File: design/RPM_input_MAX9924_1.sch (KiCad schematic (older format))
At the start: 7 parts, among them U30 MAX9924

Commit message: Footprints added to components fields
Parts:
- R215, R216: footprint SM0805 -> SM1210
- R261: footprint (none) -> SM0805
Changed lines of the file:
@@
-EESchema Schematic File Version 2  date Thu 17 Mar 2011 02:57:02 AM ART
+EESchema Schematic File Version 2  date Thu 17 Mar 2011 12:20:05 PM ART
 LIBS:power
 LIBS:freeEMS_lib
@@
 F 0 "R261" V 6980 3350 50  0000 C CNN
 F 1 "1.6k" V 6900 3350 50  0000 C CNN
+F 2 "SM0805" H 6900 3350 60  0001 C CNN
 	1    6900 3350
 	0    1    1    0
@@
 F 0 "R212" V 3380 2800 50  0000 C CNN
 F 1 "10k 1/2W" V 3300 2800 50  0000 C CNN
-F 2 "SM0805" V 1130 2600 60  0001 C CNN
+F 2 "SM1210" V 1130 2600 60  0001 C CNN
 F 4 "Stackpole" V 1130 2600 60  0001 C CNN "mfg"
 F 5 "RMCF0805JT10K0CT" V 1130 2600 60  0001 C CNN "mfg#"
@@
 F 0 "R213" V 3380 3200 50  0000 C CNN
 F 1 "10k 1/2W" V 3300 3200 50  0000 C CNN
-F 2 "SM0805" V 1130 2600 60  0001 C CNN
+F 2 "SM1210" V 1130 2600 60  0001 C CNN
 F 4 "Stackpole" V 1130 2600 60  0001 C CNN "mfg"
 F 5 "RMCF0805JT10K0CT" V 1130 2600 60  0001 C CNN "mfg#"

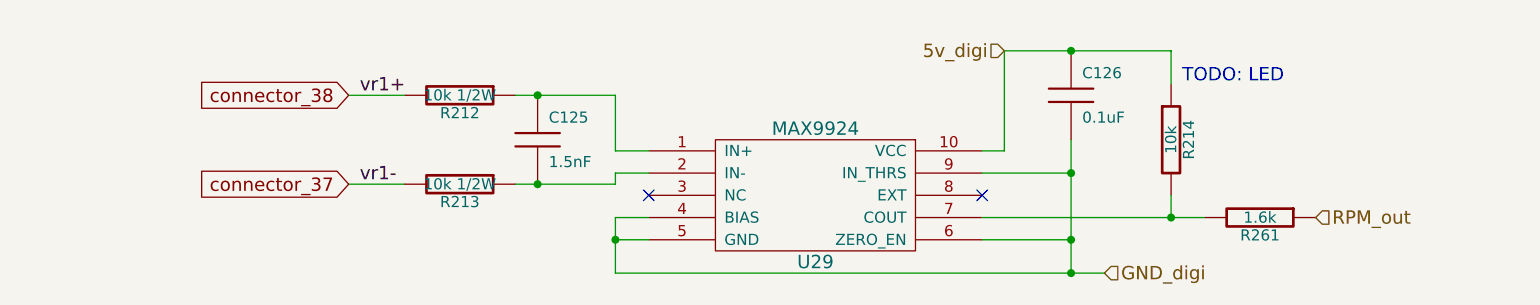
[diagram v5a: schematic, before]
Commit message: Added leds to RPM inputs
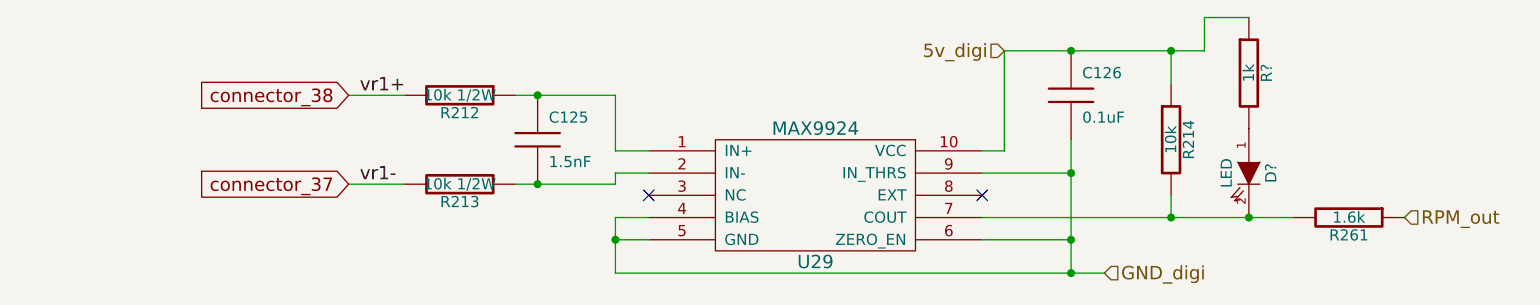
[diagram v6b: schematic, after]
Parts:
- added D?: LED, symbol LED
- added R?: 1k, symbol R
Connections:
- net 5v_digi: now also R?.1
- net at R217.2, R261.2, U30.7 (COUT): now also D?.2 (K)
- new net: D?.1 (A), R?.2
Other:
- note removed: "TODO: LED"
- moved on the sheet: R261
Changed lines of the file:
@@
-EESchema Schematic File Version 2  date Sat 19 Mar 2011 03:00:13 PM ART
+EESchema Schematic File Version 2  date Mon 21 Mar 2011 04:08:08 AM ART
 LIBS:power
 LIBS:freeEMS_lib
@@
 EELAYER END
 $Descr A4 11700 8267
-Sheet 18 55
+Sheet 19 55
 Title "Puma board"
-Date "19 mar 2011"
+Date "21 mar 2011"
 Rev "v0.02"
 Comp "diyefi.org"
@@
 Comment4 ""
 $EndDescr
-Text Notes 6550 2750 0    60   ~ 0
-TODO: LED
+Connection ~ 6850 3350
+Wire Wire Line
+	7050 3350 5650 3350
+Connection ~ 6500 2600
+Wire Wire Line
+	6650 2600 5750 2600
+Wire Wire Line
+	6650 2600 6650 2450
+Wire Wire Line
+	6650 2450 6850 2450
+Wire Wire Line
+	6050 3600 6050 3000
+Wire Wire Line
+	4000 3350 4000 3600
+Wire Wire Line
+	2800 3200 3050 3200
+Wire Wire Line
+	4000 3050 4000 2800
+Wire Wire Line
+	4000 3050 4150 3050
+Wire Wire Line
+	4000 3150 4000 3200
+Wire Wire Line
+	4000 3150 4150 3150
+Connection ~ 6500 3350
+Wire Wire Line
+	6500 3250 6500 3350
+Connection ~ 6050 3450
+Wire Wire Line
+	6050 3150 5650 3150
+Wire Wire Line
+	4000 3450 4150 3450
+Wire Wire Line
+	5650 3050 5750 3050
+Wire Wire Line
+	5750 3050 5750 2600
+Wire Wire Line
+	4000 3350 4150 3350
+Connection ~ 4000 3450
+Wire Wire Line
+	6050 3450 5650 3450
+Connection ~ 6050 3150
+Wire Wire Line
+	6500 2600 6500 2750
+Connection ~ 6050 2600
+Wire Wire Line
+	4000 3200 3550 3200
+Connection ~ 3650 3200
+Wire Wire Line
+	4000 2800 3550 2800
+Connection ~ 3650 2800
+Wire Wire Line
+	3050 2800 2800 2800
+Wire Wire Line
+	4000 3600 6200 3600
+Connection ~ 6050 3600
+$Comp
+L LED D?
+U 1 1 4D86F760
+P 6850 3150
+F 0 "D?" H 6850 3250 50  0000 C CNN
+F 1 "LED" H 6850 3050 50  0000 C CNN
+	1    6850 3150
+	0    1    1    0
+$EndComp
+$Comp
+L R R?
+U 1 1 4D86F74F
+P 6850 2700
+F 0 "R?" V 6930 2700 50  0000 C CNN
+F 1 "1k" V 6850 2700 50  0000 C CNN
+	1    6850 2700
+	1    0    0    -1
+$EndComp
 $Comp
 L R R261
 U 1 1 4D6402A4
-P 6900 3350
-F 0 "R261" V 6980 3350 50  0000 C CNN
-F 1 "1.6k" V 6900 3350 50  0000 C CNN
-F 2 "SM0805" H 6900 3350 60  0001 C CNN
-	1    6900 3350
+P 7300 3350
+F 0 "R261" V 7380 3350 50  0000 C CNN
+F 1 "1.6k" V 7300 3350 50  0000 C CNN
+F 2 "SM0805" H 7300 3350 60  0001 C CNN
+	1    7300 3350
 	0    1    1    0
 $EndComp
@@
 Text HLabel 6200 3600 2    60   Input ~ 0
 GND_digi
-Connection ~ 6050 3600
-Wire Wire Line
-	6200 3600 4000 3600
-Wire Wire Line
-	3050 2800 2800 2800
-Connection ~ 3650 2800
-Wire Wire Line
-	3550 2800 4000 2800
-Connection ~ 3650 3200
-Wire Wire Line
-	3550 3200 4000 3200
-Connection ~ 6050 2600
-Wire Wire Line
-	6500 2750 6500 2600
-Wire Wire Line
-	6500 2600 5750 2600
-Wire Wire Line
-	5650 3350 6650 3350
-Connection ~ 6050 3150
-Wire Wire Line
-	6050 3450 5650 3450
-Connection ~ 4000 3450
-Wire Wire Line
-	4150 3350 4000 3350
-Wire Wire Line
-	5750 2600 5750 3050
-Wire Wire Line
-	5750 3050 5650 3050
-Wire Wire Line
-	4000 3450 4150 3450
-Wire Wire Line
-	6050 3150 5650 3150
-Connection ~ 6050 3450
-Wire Wire Line
-	6500 3250 6500 3350
-Connection ~ 6500 3350
-Wire Wire Line
-	4150 3150 4000 3150
-Wire Wire Line
-	4000 3150 4000 3200
-Wire Wire Line
-	4150 3050 4000 3050
-Wire Wire Line
-	4000 3050 4000 2800
-Wire Wire Line
-	2800 3200 3050 3200
-Wire Wire Line
-	4000 3350 4000 3600
-Wire Wire Line
-	6050 3600 6050 3000
-Text HLabel 7150 3350 2    60   Input ~ 0
+Text HLabel 7550 3350 2    60   Input ~ 0
 RPM_out
 Text HLabel 5750 2600 0    60   Input ~ 0

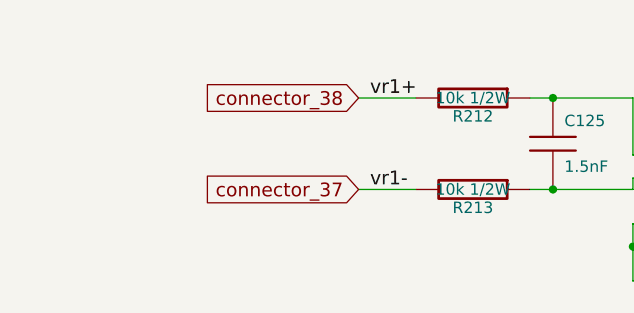
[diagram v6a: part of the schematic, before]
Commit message: Added front-side capacitors on RPM circuits
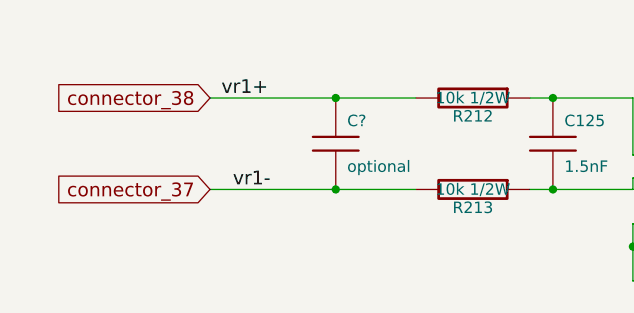
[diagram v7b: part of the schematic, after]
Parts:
- added C?: optional, symbol C
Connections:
- net connector_37: now also C?.2
- net connector_38: now also C?.1
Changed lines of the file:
@@
-EESchema Schematic File Version 2  date Mon 21 Mar 2011 04:08:08 AM ART
+EESchema Schematic File Version 2  date Tue 22 Mar 2011 12:18:09 AM ART
 LIBS:power
 LIBS:freeEMS_lib
@@
 Sheet 19 55
 Title "Puma board"
-Date "21 mar 2011"
+Date "22 mar 2011"
 Rev "v0.02"
 Comp "diyefi.org"
@@
 Comment4 ""
 $EndDescr
+Connection ~ 2700 3200
+Wire Wire Line
+	2150 2800 3050 2800
 Connection ~ 6850 3350
 Wire Wire Line
@@
 Wire Wire Line
 	4000 3350 4000 3600
-Wire Wire Line
-	2800 3200 3050 3200
 Wire Wire Line
 	4000 3050 4000 2800
@@
 Connection ~ 3650 2800
 Wire Wire Line
-	3050 2800 2800 2800
-Wire Wire Line
 	4000 3600 6200 3600
 Connection ~ 6050 3600
+Wire Wire Line
+	2150 3200 3050 3200
+Connection ~ 2700 2800
+$Comp
+L C C?
+U 1 1 4D881199
+P 2700 3000
+F 0 "C?" H 2750 3100 50  0000 L CNN
+F 1 "optional" H 2750 2900 50  0000 L CNN
+	1    2700 3000
+	1    0    0    -1
+$EndComp
 $Comp
 L LED D?
@@
 	0    1    1    0
 $EndComp
-Text Label 2850 3200 0    60   ~ 0
+Text Label 2250 3200 0    60   ~ 0
 vr1-
-Text Label 2850 2800 0    60   ~ 0
+Text Label 2200 2800 0    60   ~ 0
 vr1+
-Text GLabel 2800 2800 0    60   Input ~ 0
+Text GLabel 2150 2800 0    60   Input ~ 0
 connector_38
-Text GLabel 2800 3200 0    60   Input ~ 0
+Text GLabel 2150 3200 0    60   Input ~ 0
 connector_37
 Text HLabel 6200 3600 2    60   Input ~ 0

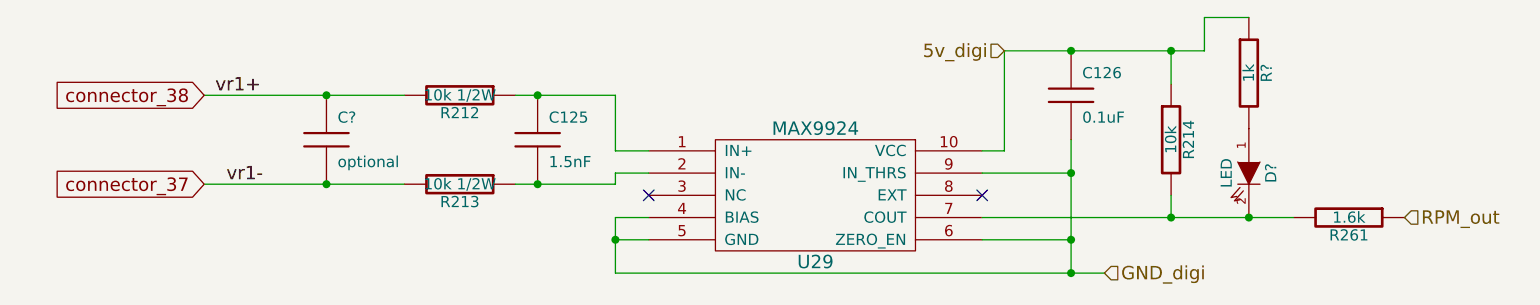
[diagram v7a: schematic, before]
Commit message: Replaced 1/2W resistors by a couple of 1/4W (RPM circuitry)
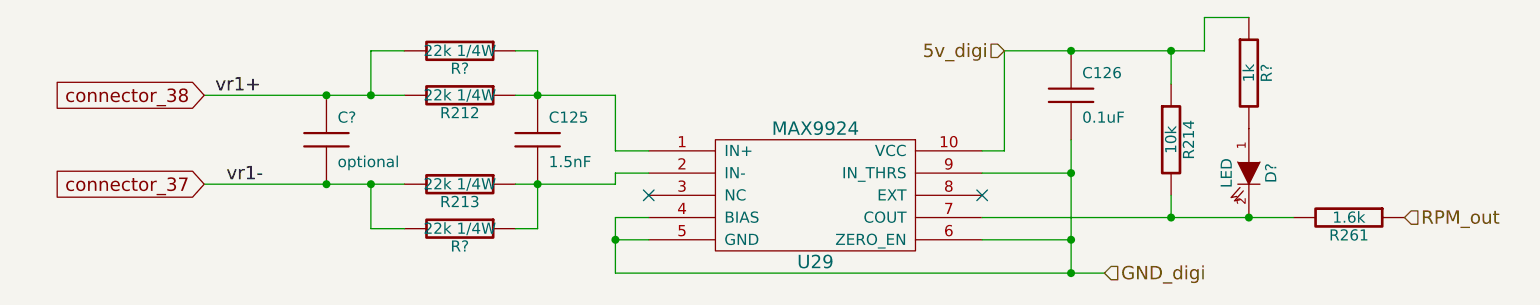
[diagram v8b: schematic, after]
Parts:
- added R? (x2): 22k 1/4W, symbol R
- R215, R216: value 10k 1/2W -> 22k 1/4W
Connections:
- net connector_37: now also R?.2
- net connector_38: now also R?.2
- net at C127.1, R215.1, U30.1 (IN+): now also R?.1
- net at C127.2, R216.1, U30.2 (IN-): now also R?.1
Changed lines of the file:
@@
-EESchema Schematic File Version 2  date Tue 22 Mar 2011 12:18:09 AM ART
+EESchema Schematic File Version 2  date Tue 22 Mar 2011 12:22:23 AM ART
 LIBS:power
 LIBS:freeEMS_lib
@@
 Comment4 ""
 $EndDescr
+Wire Wire Line
+	3650 3200 3650 3400
+Wire Wire Line
+	3650 3400 3550 3400
+Connection ~ 2900 2800
+Wire Wire Line
+	2900 2800 2900 2600
+Wire Wire Line
+	2900 2600 3050 2600
 Connection ~ 2700 3200
 Wire Wire Line
@@
 	2150 3200 3050 3200
 Connection ~ 2700 2800
+Wire Wire Line
+	3550 2600 3650 2600
+Wire Wire Line
+	3650 2600 3650 2800
+Wire Wire Line
+	3050 3400 2900 3400
+Wire Wire Line
+	2900 3400 2900 3200
+Connection ~ 2900 3200
+$Comp
+L R R?
+U 1 1 4D881558
+P 3300 3400
+F 0 "R?" V 3380 3400 50  0000 C CNN
+F 1 "22k 1/4W" V 3300 3400 50  0000 C CNN
+	1    3300 3400
+	0    1    1    0
+$EndComp
+$Comp
+L R R?
+U 1 1 4D881553
+P 3300 2600
+F 0 "R?" V 3380 2600 50  0000 C CNN
+F 1 "22k 1/4W" V 3300 2600 50  0000 C CNN
+	1    3300 2600
+	0    1    1    0
+$EndComp
 $Comp
 L C C?
@@
 AR Path="/4C94FDB6/4C94FEDF" Ref="R212"  Part="1"
 F 0 "R212" V 3380 2800 50  0000 C CNN
-F 1 "10k 1/2W" V 3300 2800 50  0000 C CNN
+F 1 "22k 1/4W" V 3300 2800 50  0000 C CNN
 F 2 "SM1210" V 1130 2600 60  0001 C CNN
 F 4 "Stackpole" V 1130 2600 60  0001 C CNN "mfg"
@@
 AR Path="/4C94FDB6/4CCADF73" Ref="R213"  Part="1"
 F 0 "R213" V 3380 3200 50  0000 C CNN
-F 1 "10k 1/2W" V 3300 3200 50  0000 C CNN
+F 1 "22k 1/4W" V 3300 3200 50  0000 C CNN
 F 2 "SM1210" V 1130 2600 60  0001 C CNN
 F 4 "Stackpole" V 1130 2600 60  0001 C CNN "mfg"
